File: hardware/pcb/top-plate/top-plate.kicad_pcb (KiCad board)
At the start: 2 copper layers, 65 x 120 mm, 4 parts

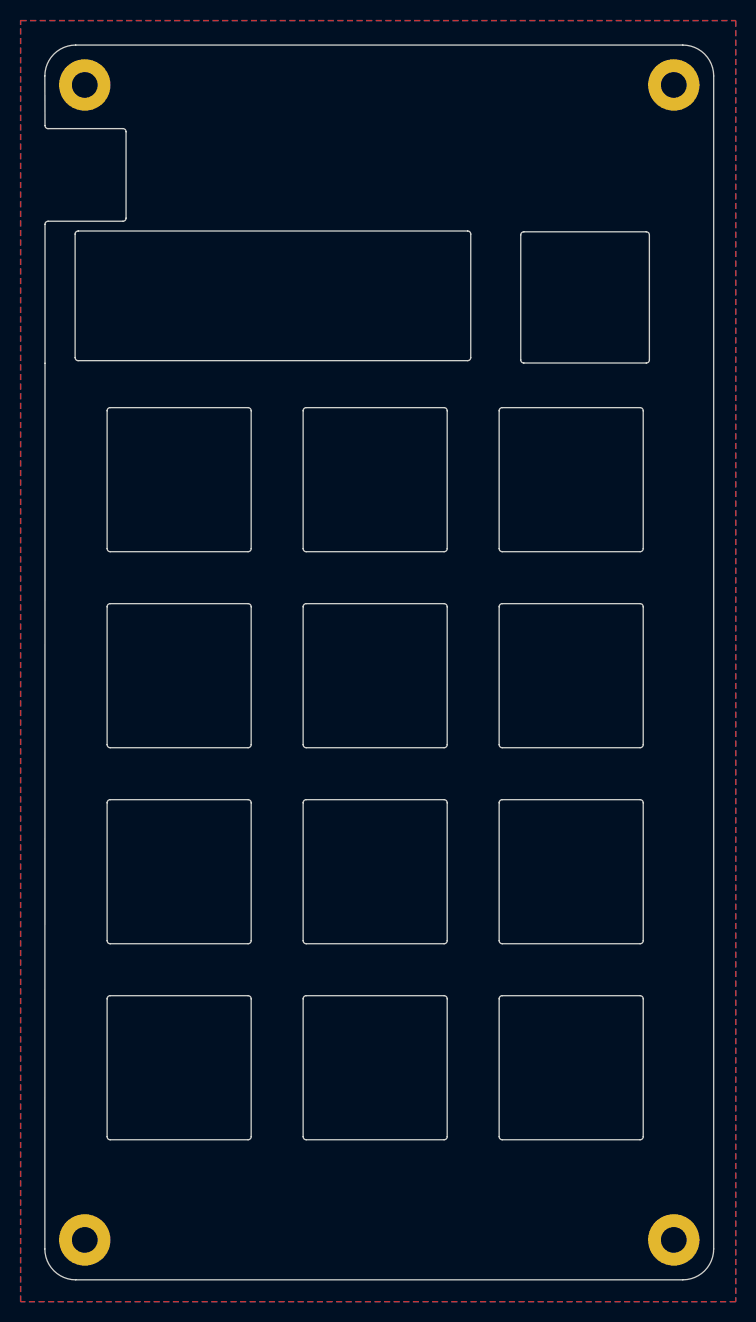
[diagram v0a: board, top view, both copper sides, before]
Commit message: Optimize routing and improve grounding
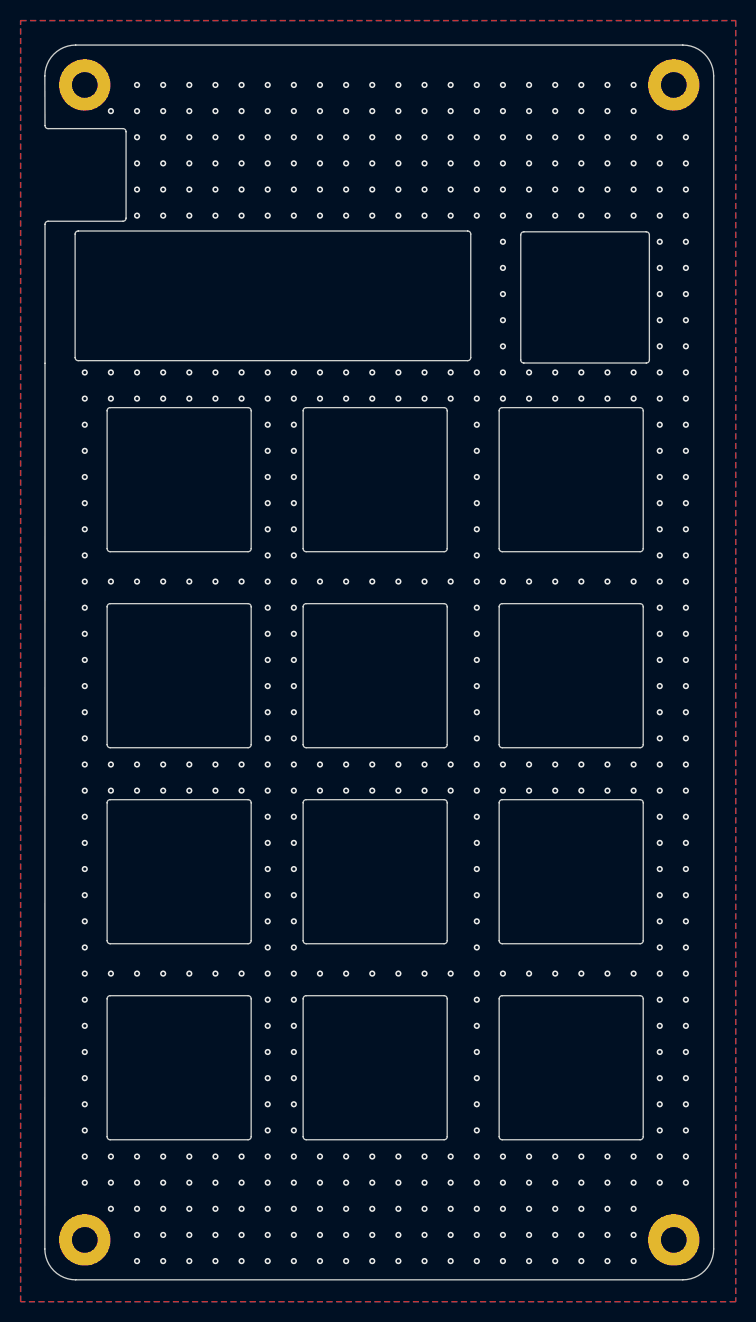
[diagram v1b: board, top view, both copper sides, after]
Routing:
- net GND: vias 0 -> 541

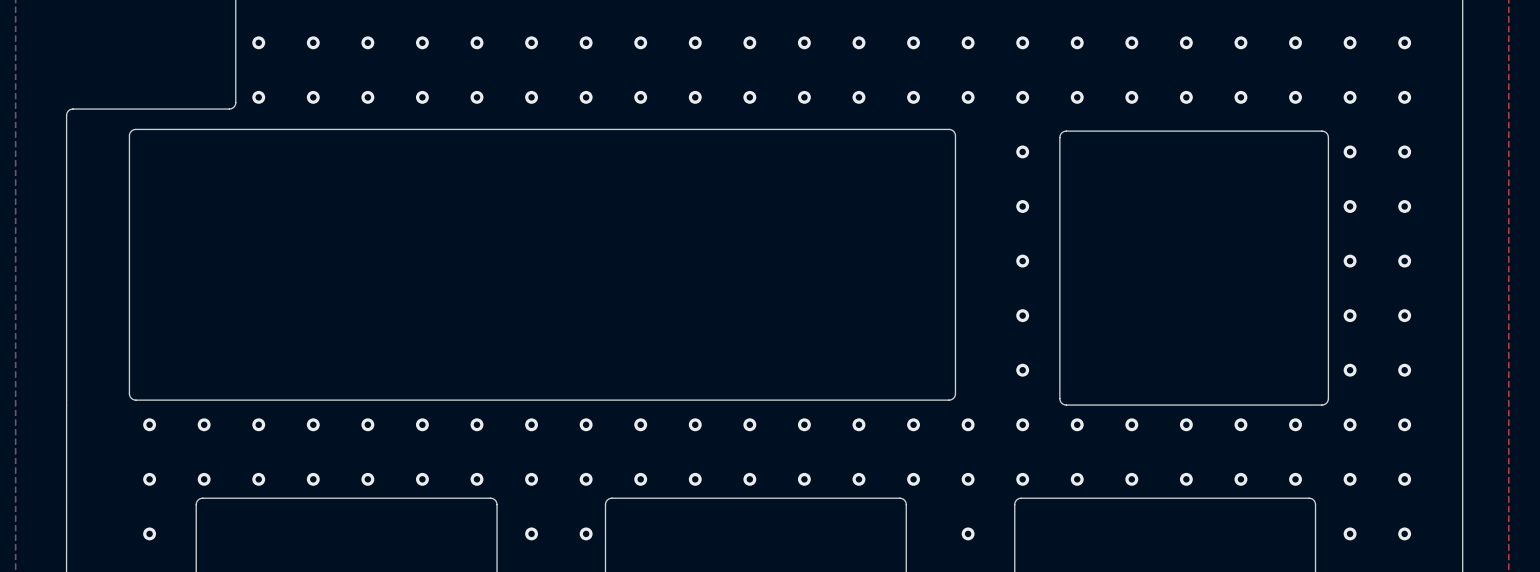
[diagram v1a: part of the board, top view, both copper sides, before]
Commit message: Add SOT95P280X145-6N footprint to Bottom-Footprints library
- Created a new footprint for the SOT95P280X145-6N component.
- Included necessary pads, silkscreen, and fabrication lines.
- Added 3D model reference for TPS22918DBVR.
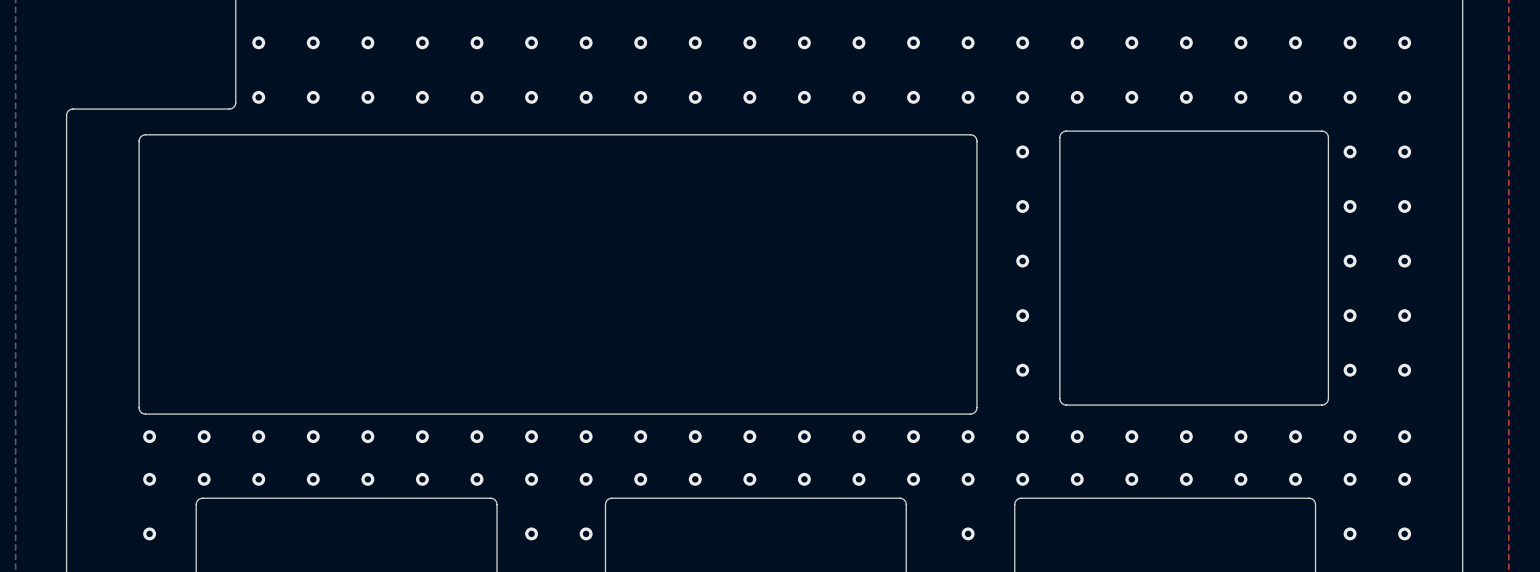
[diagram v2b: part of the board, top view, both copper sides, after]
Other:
- outline, holes or cut-outs redrawn

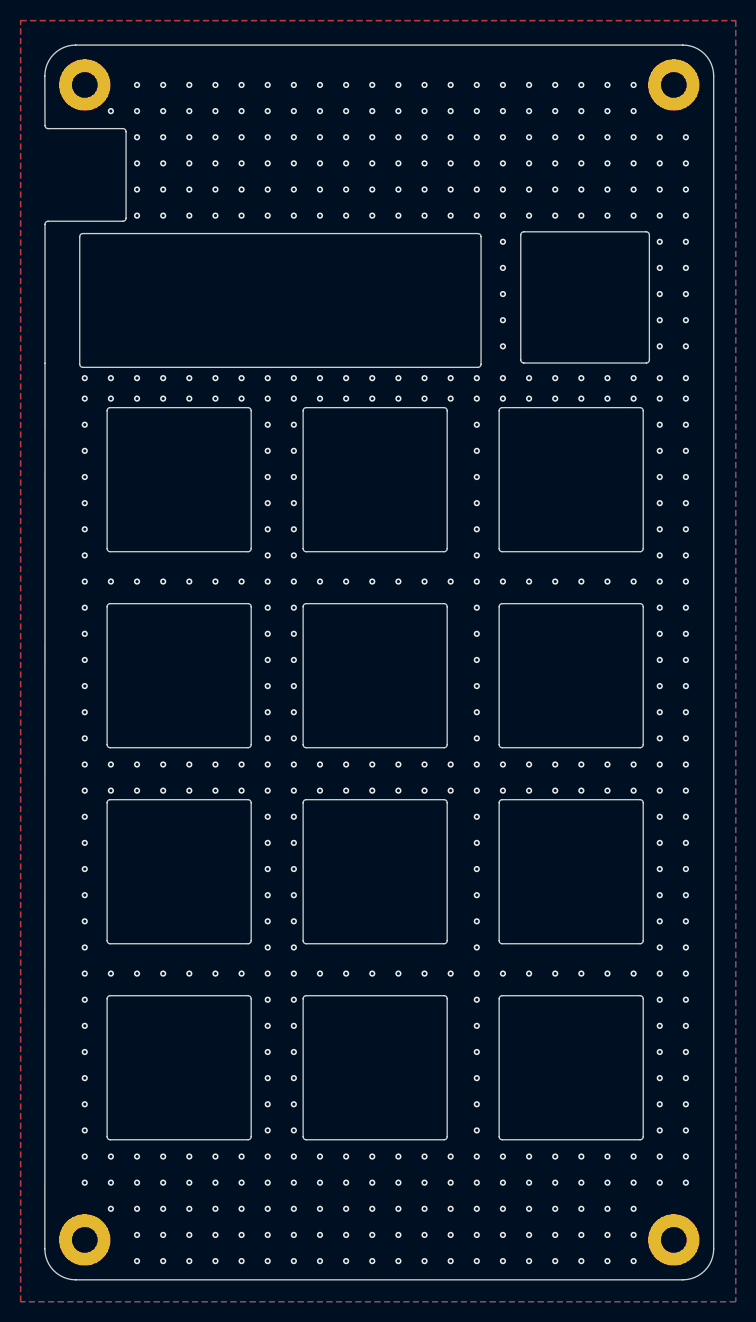
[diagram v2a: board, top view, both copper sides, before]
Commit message: update documentation images, remove copper pours and vias from top plate, minor fixes
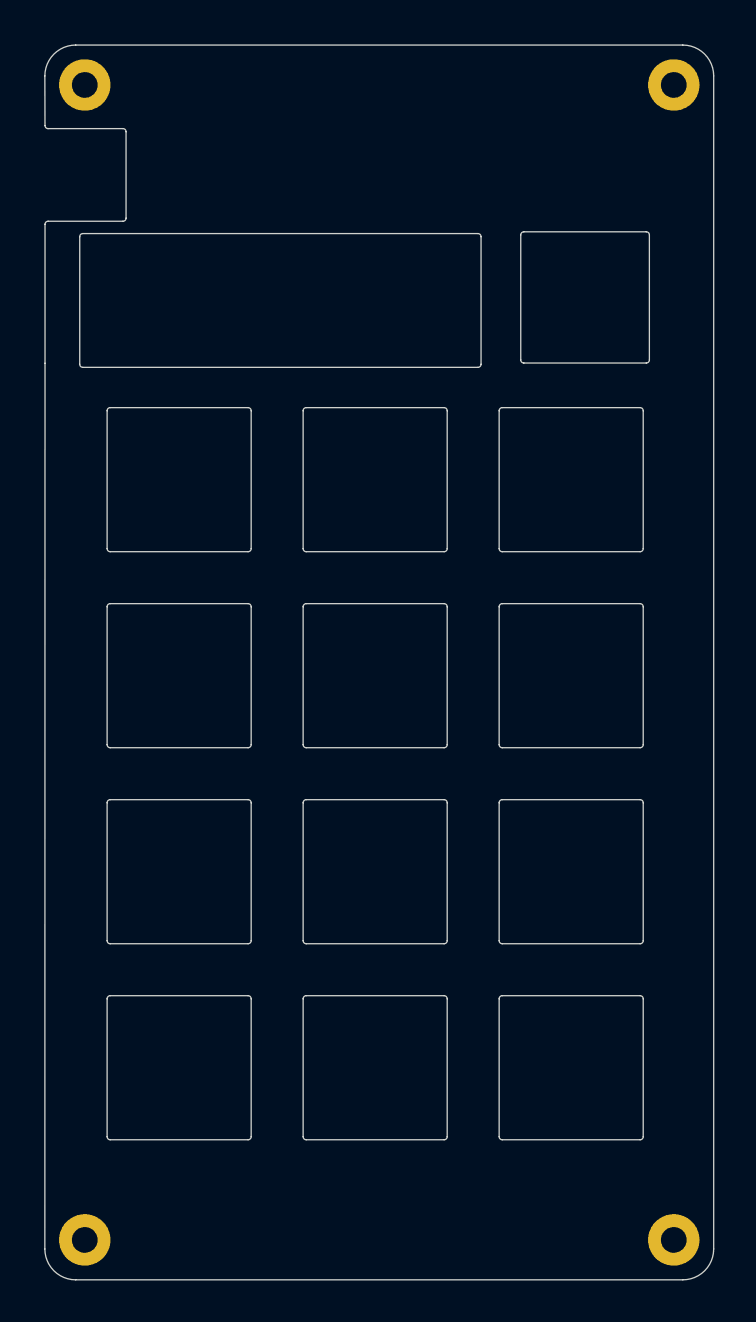
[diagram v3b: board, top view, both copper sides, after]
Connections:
- H1 pad 1: GND -> unconnected-(H1-Pad1)
- H2 pad 1: GND -> unconnected-(H2-Pad1)
- H3 pad 1: GND -> unconnected-(H3-Pad1)
- H4 pad 1: GND -> unconnected-(H4-Pad1)
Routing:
- net GND: vias 541 -> 0
- removed copper zone on B.Cu, net GND
- removed copper zone on F.Cu, net GND

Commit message: changed m2.5 mh to m2, added screws and nuts to enclosure.FCStd
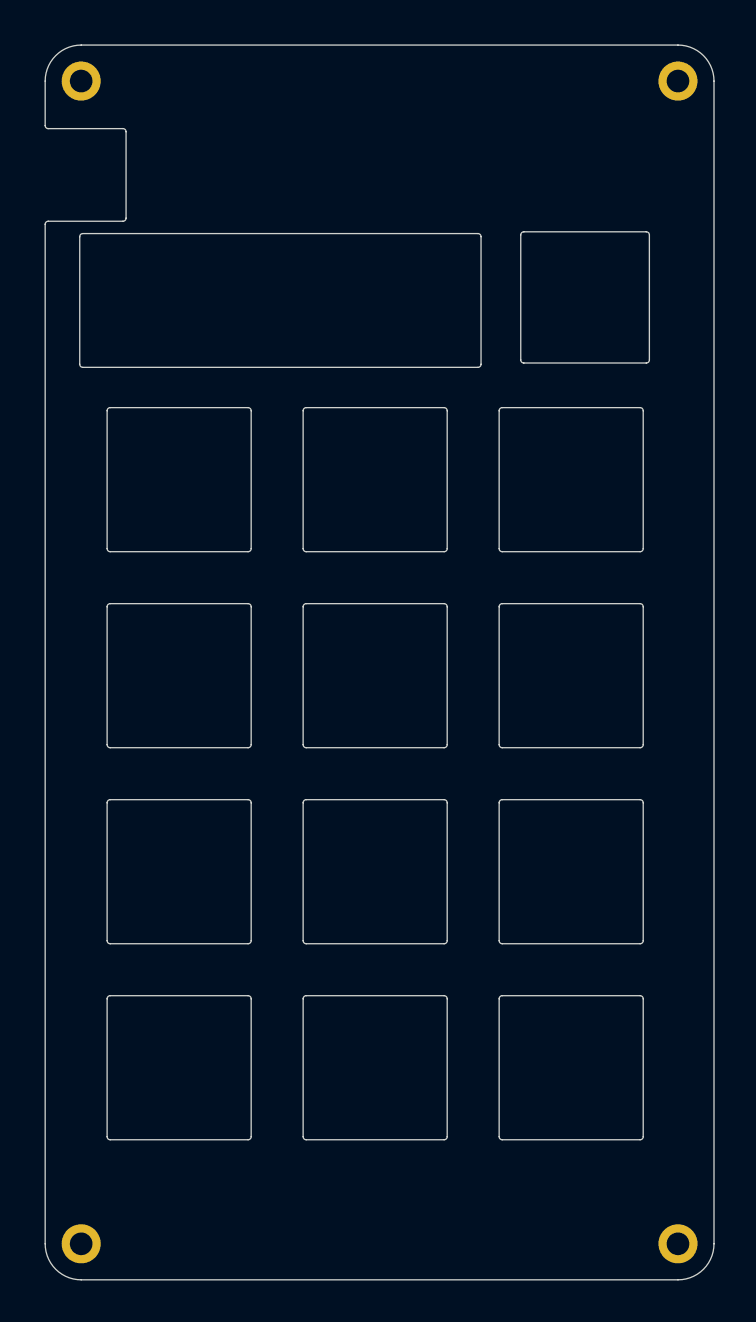
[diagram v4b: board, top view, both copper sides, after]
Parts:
- H1, H2, H3, H4: footprint MountingHole:MountingHole_2.5mm_Pad -> MountingHole:MountingHole_2.2mm_M2_DIN965_Pad
- moved H4 0.56 mm to (146.6, 148.4)
- moved H1 0.56 mm to (146.6, 35.4)
- moved H3 0.51 mm to (88.6, 148.4)
- moved H2 0.51 mm to (88.6, 35.4)
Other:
- outline, holes or cut-outs redrawn

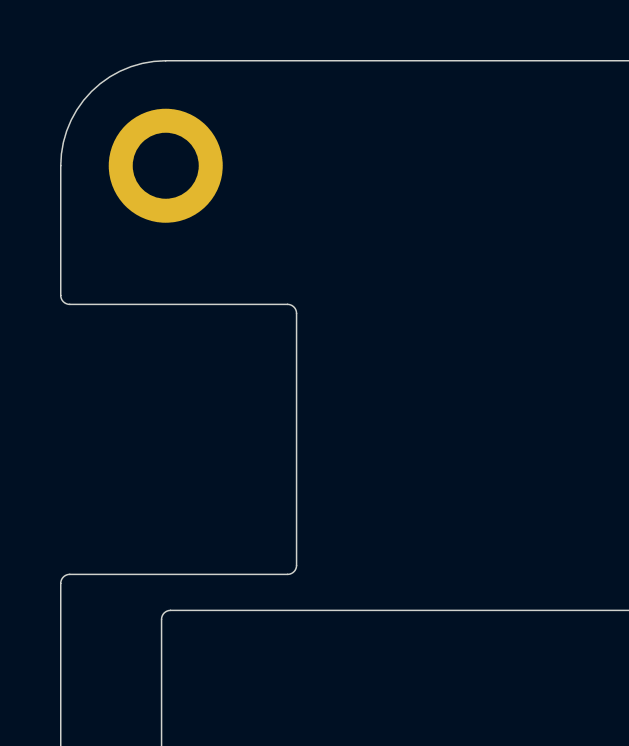
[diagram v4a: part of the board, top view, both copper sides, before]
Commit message: fixed positioning issues, changed the type of nuts holding the pcb
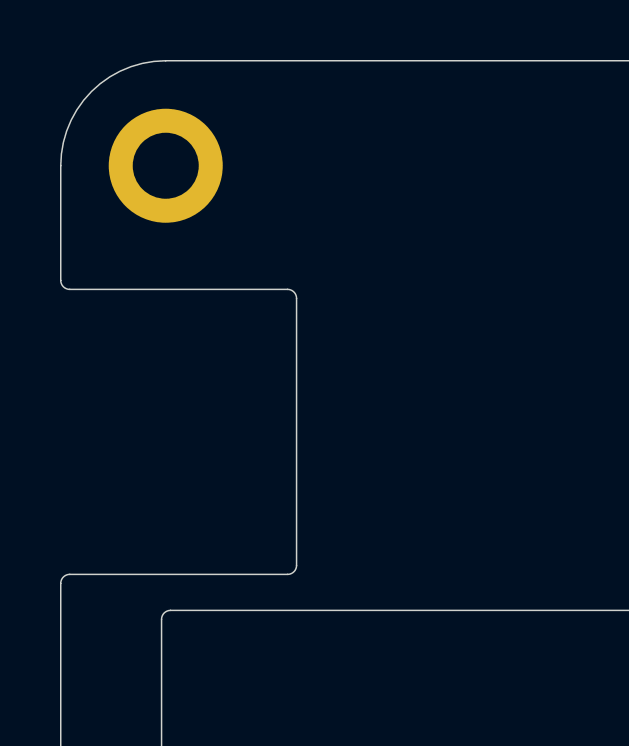
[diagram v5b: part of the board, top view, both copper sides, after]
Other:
- outline, holes or cut-outs redrawn
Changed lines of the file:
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@@
 	)
 	(gr_line
-		(start 92.7 40)
-		(end 85.43977 40)
+		(start 92.7 39.5)
+		(end 85.43977 39.5)
 		(stroke
 			(width 0.05)
@@
 	)
 	(gr_arc
+		(start 92.7 39.5)
+		(mid 92.912132 39.587868)
+		(end 93 39.8)
+		(stroke
+			(width 0.05)
+			(type default)
+		)
+		(layer "Edge.Cuts")
+	)
+	(gr_arc
 		(start 142.959541 124.26618)
 		(mid 143.171654 124.354061)
@@
 	)
 	(gr_line
-		(start 93 40.3)
+		(start 93 39.8)
 		(end 93 48.7)
 		(stroke
@@
 		(layer "Edge.Cuts")
 	)
-	(gr_arc
-		(start 85.43977 40)
-		(mid 85.227657 39.912121)
-		(end 85.13977 39.7)
-		(stroke
-			(width 0.05)
-			(type default)
-		)
-		(layer "Edge.Cuts")
-	)
 	(gr_line
 		(start 91.159541 137.96618)
@@
 		(layer "Edge.Cuts")
 	)
+	(gr_arc
+		(start 85.43977 39.5)
+		(mid 85.227638 39.412132)
+		(end 85.13977 39.2)
+		(stroke
+			(width 0.05)
+			(type default)
+		)
+		(layer "Edge.Cuts")
+	)
 	(gr_line
 		(start 129.259541 99.86618)
@@
 	)
 	(gr_line
-		(start 85.13977 39.7)
+		(start 85.13977 39.2)
 		(end 85.13977 35.37884)
 		(stroke
@@
 		(stroke
 			(width 0.05)
-			(type default)
-		)
-		(layer "Edge.Cuts")
-	)
-	(gr_arc
-		(start 92.7 40)
-		(mid 92.912132 40.087868)
-		(end 93 40.3)
-		(stroke
-			(width 0.05)
